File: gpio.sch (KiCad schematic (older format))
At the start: 1 part, among them U1 LFE5U-85F-6BG381C

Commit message: More fixes
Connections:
- net AUDIO_L0 renamed LTDC_TO_FPGA_DE
- net AUDIO_L1 renamed LTDC_TO_FPGA_B6
- net AUDIO_L2 renamed LTDC_TO_FPGA_G4
- net AUDIO_R0 renamed LTDC_TO_FPGA_G2
- net AUDIO_R2 renamed LTDC_TO_FPGA_B5
- net AUDIO_V2 renamed LTDC_TO_FPGA_B4
- net GN10 renamed LTDC_TO_FPGA_B7
- net GN11 renamed LTDC_TO_FPGA_B3
- net GN9 renamed LTDC_TO_FPGA_R6
- net GP11 renamed LTDC_TO_FPGA_G5
- net GP12 renamed LTDC_TO_FPGA_CLK
- net GP9 renamed LTDC_TO_FPGA_G7
- net LED1 renamed LTDC_TO_FPGA_R7
- net LED2 renamed LTDC_TO_FPGA_HSYNC
- net LED3 renamed LTDC_TO_FPGA_VSYNC
- net LED4 renamed LTDC_TO_FPGA_R4
- net LED6 renamed LTDC_TO_FPGA_R5
- net LED7 renamed LTDC_TO_FPGA_R3
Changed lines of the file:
@@
 Text GLabel 4200 4900 0    60   Input ~ 0
 GP13
-Text GLabel 4200 5100 0    60   Input ~ 0
-GP12
 Text GLabel 5700 5100 2    60   Input ~ 0
 GN12
-Text GLabel 5700 4300 2    60   Input ~ 0
-GN11
-Text GLabel 4200 4300 0    60   Input ~ 0
-GP11
-Text GLabel 5700 4500 2    60   Input ~ 0
-GN9
-Text GLabel 4200 4500 0    60   Input ~ 0
-GP9
-Text GLabel 5700 3900 2    60   Input ~ 0
-GN10
 Text GLabel 5700 3700 2    60   Input ~ 0
 GN8
@@
 Text GLabel 4200 2100 0    60   Input ~ 0
 GP3
-Text GLabel 4200 4100 0    60   Input ~ 0
-AUDIO_L0
-Text GLabel 5700 4000 2    60   Input ~ 0
-AUDIO_L1
-Text GLabel 4200 4000 0    60   Input ~ 0
-AUDIO_L2
 Text GLabel 5700 3800 2    60   Input ~ 0
 AUDIO_L3
-Text GLabel 4200 3800 0    60   Input ~ 0
-AUDIO_R0
 Text GLabel 4200 3600 0    60   Input ~ 0
 AUDIO_R1
-Text GLabel 5700 4100 2    60   Input ~ 0
-AUDIO_R2
 Text GLabel 5700 3600 2    60   Input ~ 0
 AUDIO_R3
 Text GLabel 5700 5000 2    60   Input ~ 0
 LED5
-Text GLabel 4200 4700 0    60   Input ~ 0
-LED2
-Text GLabel 4200 4600 0    60   Input ~ 0
-LED3
-Text GLabel 5700 4700 2    60   Input ~ 0
-LED4
-Text GLabel 5700 4400 2    60   Input ~ 0
-LED1
-Text GLabel 5700 4600 2    60   Input ~ 0
-LED6
-Text GLabel 5700 4800 2    60   Input ~ 0
-LED7
 Text Notes 950  7550 0    60   ~ 0
 GPIO route only A/B pairs as those are differential bidirectional\ndon't route C/D pairs to GPIO as those can be differential input only\nBANK0,1 are single-ended (non-differential)
@@
 Text GLabel 4200 2700 0    60   Input ~ 0
 SW4
-Text GLabel 4200 4200 0    60   Input ~ 0
-AUDIO_V3
-Text GLabel 5700 4200 2    60   Input ~ 0
-AUDIO_V2
 Text GLabel 4200 5000 0    60   Input ~ 0
 AUDIO_V1
@@
 NoConn ~ 4200 3100
 NoConn ~ 5700 3000
-Text GLabel 6950 4800 2    60   Input ~ 0
+Text GLabel 5700 4800 2    60   Input ~ 0
 LTDC_TO_FPGA_R3
-Text GLabel 6950 4700 2    60   Input ~ 0
+Text GLabel 5700 4700 2    60   Input ~ 0
 LTDC_TO_FPGA_R4
-Text GLabel 6950 4600 2    60   Input ~ 0
+Text GLabel 5700 4600 2    60   Input ~ 0
 LTDC_TO_FPGA_R5
-Text GLabel 6950 4500 2    60   Input ~ 0
+Text GLabel 5700 4500 2    60   Input ~ 0
 LTDC_TO_FPGA_R6
-Text GLabel 6950 4400 2    60   Input ~ 0
+Text GLabel 5700 4400 2    60   Input ~ 0
 LTDC_TO_FPGA_R7
 Text GLabel 4200 3900 0    60   Input ~ 0
 LTDC_TO_FPGA_G3
-Text GLabel 2550 4000 0    60   Input ~ 0
+Text GLabel 4200 4000 0    60   Input ~ 0
 LTDC_TO_FPGA_G4
-Text GLabel 2550 4300 0    60   Input ~ 0
+Text GLabel 4200 4300 0    60   Input ~ 0
 LTDC_TO_FPGA_G5
 Text GLabel 4200 4400 0    60   Input ~ 0
 LTDC_TO_FPGA_G6
-Text GLabel 2550 4500 0    60   Input ~ 0
+Text GLabel 4200 4500 0    60   Input ~ 0
 LTDC_TO_FPGA_G7
-Text GLabel 6950 3900 2    60   Input ~ 0
+Text GLabel 5700 3900 2    60   Input ~ 0
 LTDC_TO_FPGA_B7
-Text GLabel 6950 4000 2    60   Input ~ 0
+Text GLabel 5700 4000 2    60   Input ~ 0
 LTDC_TO_FPGA_B6
-Text GLabel 6950 4100 2    60   Input ~ 0
+Text GLabel 5700 4100 2    60   Input ~ 0
 LTDC_TO_FPGA_B5
-Text GLabel 6950 4200 2    60   Input ~ 0
+Text GLabel 5700 4200 2    60   Input ~ 0
 LTDC_TO_FPGA_B4
-Text GLabel 6950 4300 2    60   Input ~ 0
+Text GLabel 5700 4300 2    60   Input ~ 0
 LTDC_TO_FPGA_B3
-Text GLabel 2550 3800 0    60   Input ~ 0
+Text GLabel 4200 3800 0    60   Input ~ 0
 LTDC_TO_FPGA_G2
-Text GLabel 2550 5100 0    60   Input ~ 0
+Text GLabel 4200 5100 0    60   Input ~ 0
 LTDC_TO_FPGA_CLK
-Text GLabel 2550 4100 0    60   Input ~ 0
+Text GLabel 4200 4100 0    60   Input ~ 0
 LTDC_TO_FPGA_DE
-Text GLabel 2550 4700 0    60   Input ~ 0
+Text GLabel 4200 4700 0    60   Input ~ 0
 LTDC_TO_FPGA_HSYNC
-Text GLabel 2550 4600 0    60   Input ~ 0
+Text GLabel 4200 4600 0    60   Input ~ 0
 LTDC_TO_FPGA_VSYNC
-Text GLabel 2750 5100 2    60   Input ~ 0
-GP12
-Wire Wire Line
-	2750 5100 2550 5100
-Text GLabel 2650 3800 2    60   Input ~ 0
-AUDIO_R0
-Text GLabel 2650 4000 2    60   Input ~ 0
-AUDIO_L2
-Text GLabel 2650 4100 2    60   Input ~ 0
-AUDIO_L0
-Text GLabel 2650 4300 2    60   Input ~ 0
-GP11
-Text GLabel 2650 4500 2    60   Input ~ 0
-GP9
-Text GLabel 2650 4600 2    60   Input ~ 0
-LED3
-Text GLabel 2650 4700 2    60   Input ~ 0
-LED2
-Wire Wire Line
-	2550 3800 2650 3800
-Wire Wire Line
-	2550 4000 2650 4000
-Wire Wire Line
-	2650 4100 2550 4100
-Wire Wire Line
-	2550 4300 2650 4300
-Wire Wire Line
-	2550 4500 2650 4500
-Wire Wire Line
-	2650 4600 2550 4600
-Wire Wire Line
-	2550 4700 2650 4700
-Text GLabel 6850 3900 0    60   Input ~ 0
-GN10
-Text GLabel 6850 4000 0    60   Input ~ 0
-AUDIO_L1
-Text GLabel 6850 4100 0    60   Input ~ 0
-AUDIO_R2
-Text GLabel 6850 4200 0    60   Input ~ 0
-AUDIO_V2
-Text GLabel 6850 4300 0    60   Input ~ 0
-GN11
-Text GLabel 6850 4400 0    60   Input ~ 0
-LED1
-Text GLabel 6850 4500 0    60   Input ~ 0
-GN9
-Text GLabel 6850 4600 0    60   Input ~ 0
-LED6
-Text GLabel 6850 4700 0    60   Input ~ 0
-LED4
-Text GLabel 6850 4800 0    60   Input ~ 0
-LED7
-Wire Wire Line
-	6850 3900 6950 3900
-Wire Wire Line
-	6850 4000 6950 4000
-Wire Wire Line
-	6850 4100 6950 4100
-Wire Wire Line
-	6850 4200 6950 4200
-Wire Wire Line
-	6850 4300 6950 4300
-Wire Wire Line
-	6850 4400 6950 4400
-Wire Wire Line
-	6850 4500 6950 4500
-Wire Wire Line
-	6850 4600 6950 4600
-Wire Wire Line
-	6850 4700 6950 4700
-Wire Wire Line
-	6850 4800 6950 4800
 Text GLabel 4100 2800 0    60   Input ~ 0
 LTDC_FROM_FPGA_R3
@@
 Text GLabel 5700 2200 2    60   Input ~ 0
 LTDC_FROM_FPGA_R5
+Text GLabel 4200 4200 0    60   Input ~ 0
+AUDIO_V3
 $EndSCHEMATC

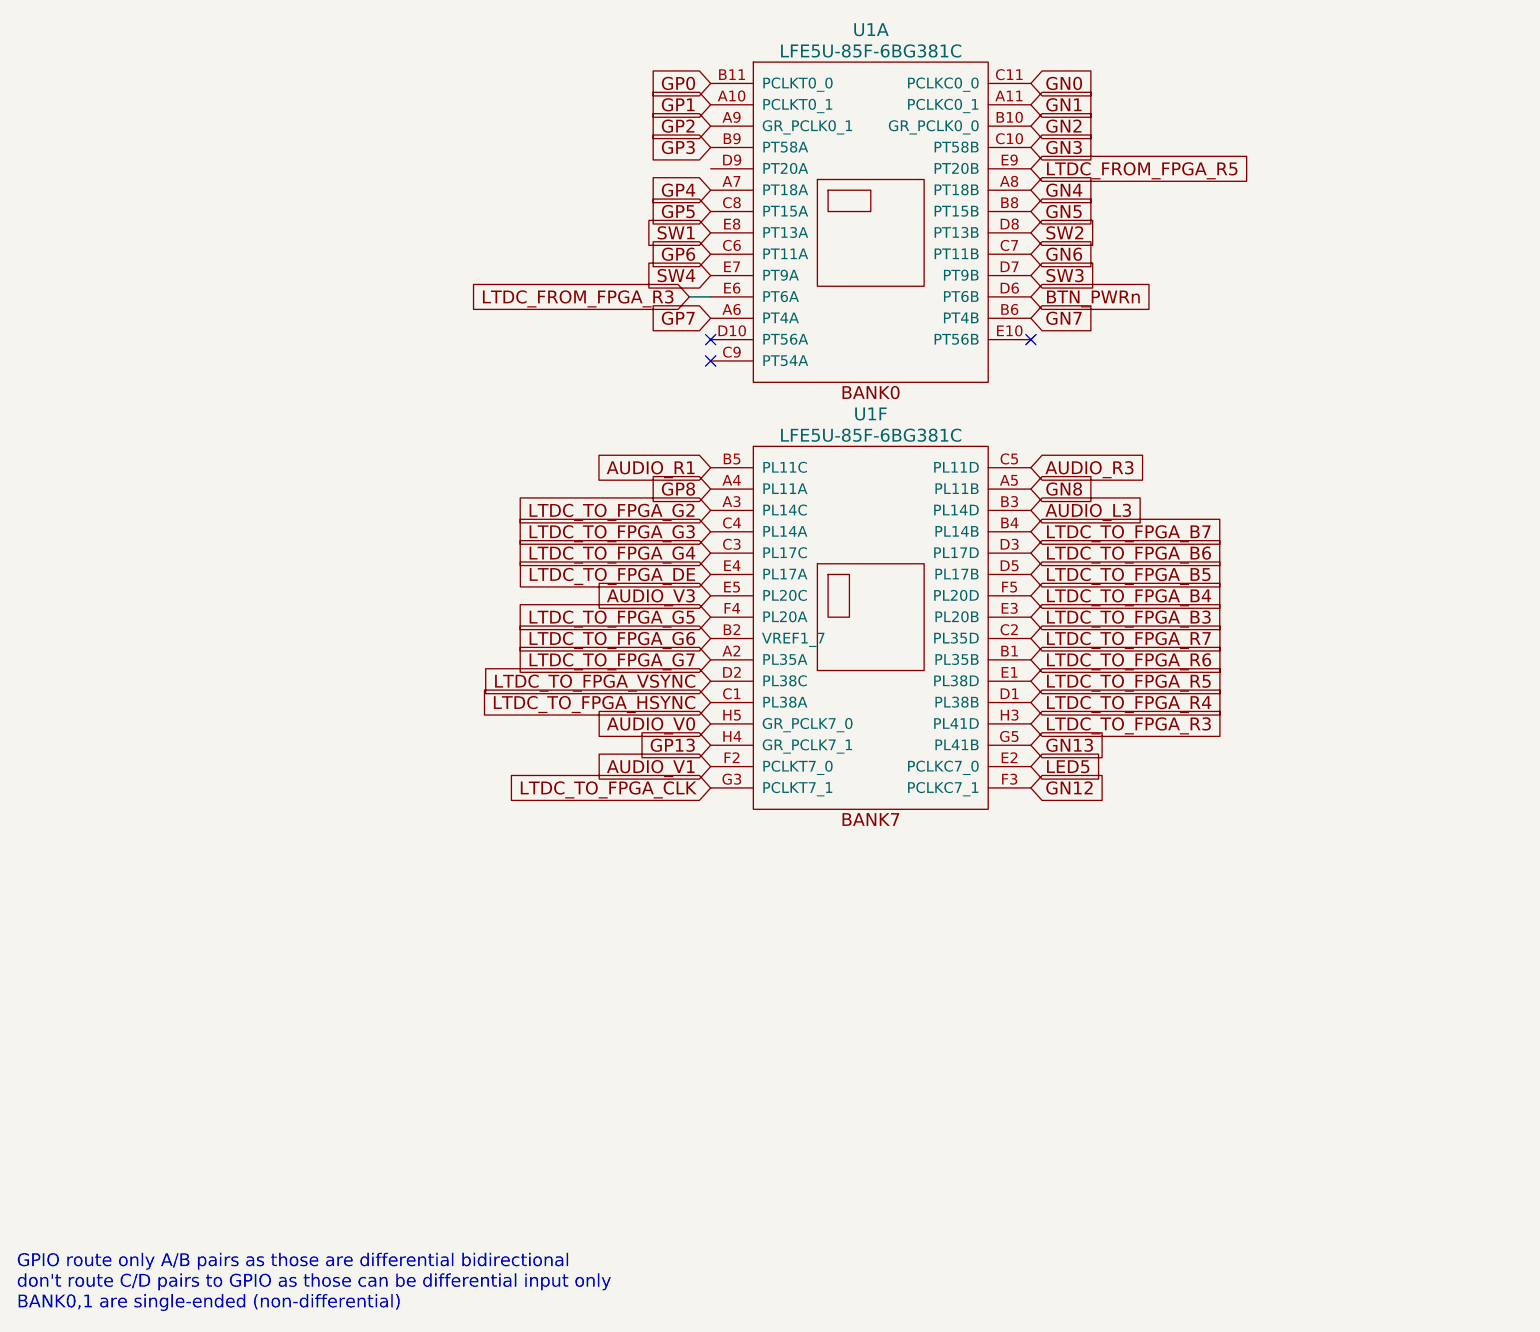
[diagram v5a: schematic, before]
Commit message: Adding all SPI to FPGA resorting LCD TO FPGA
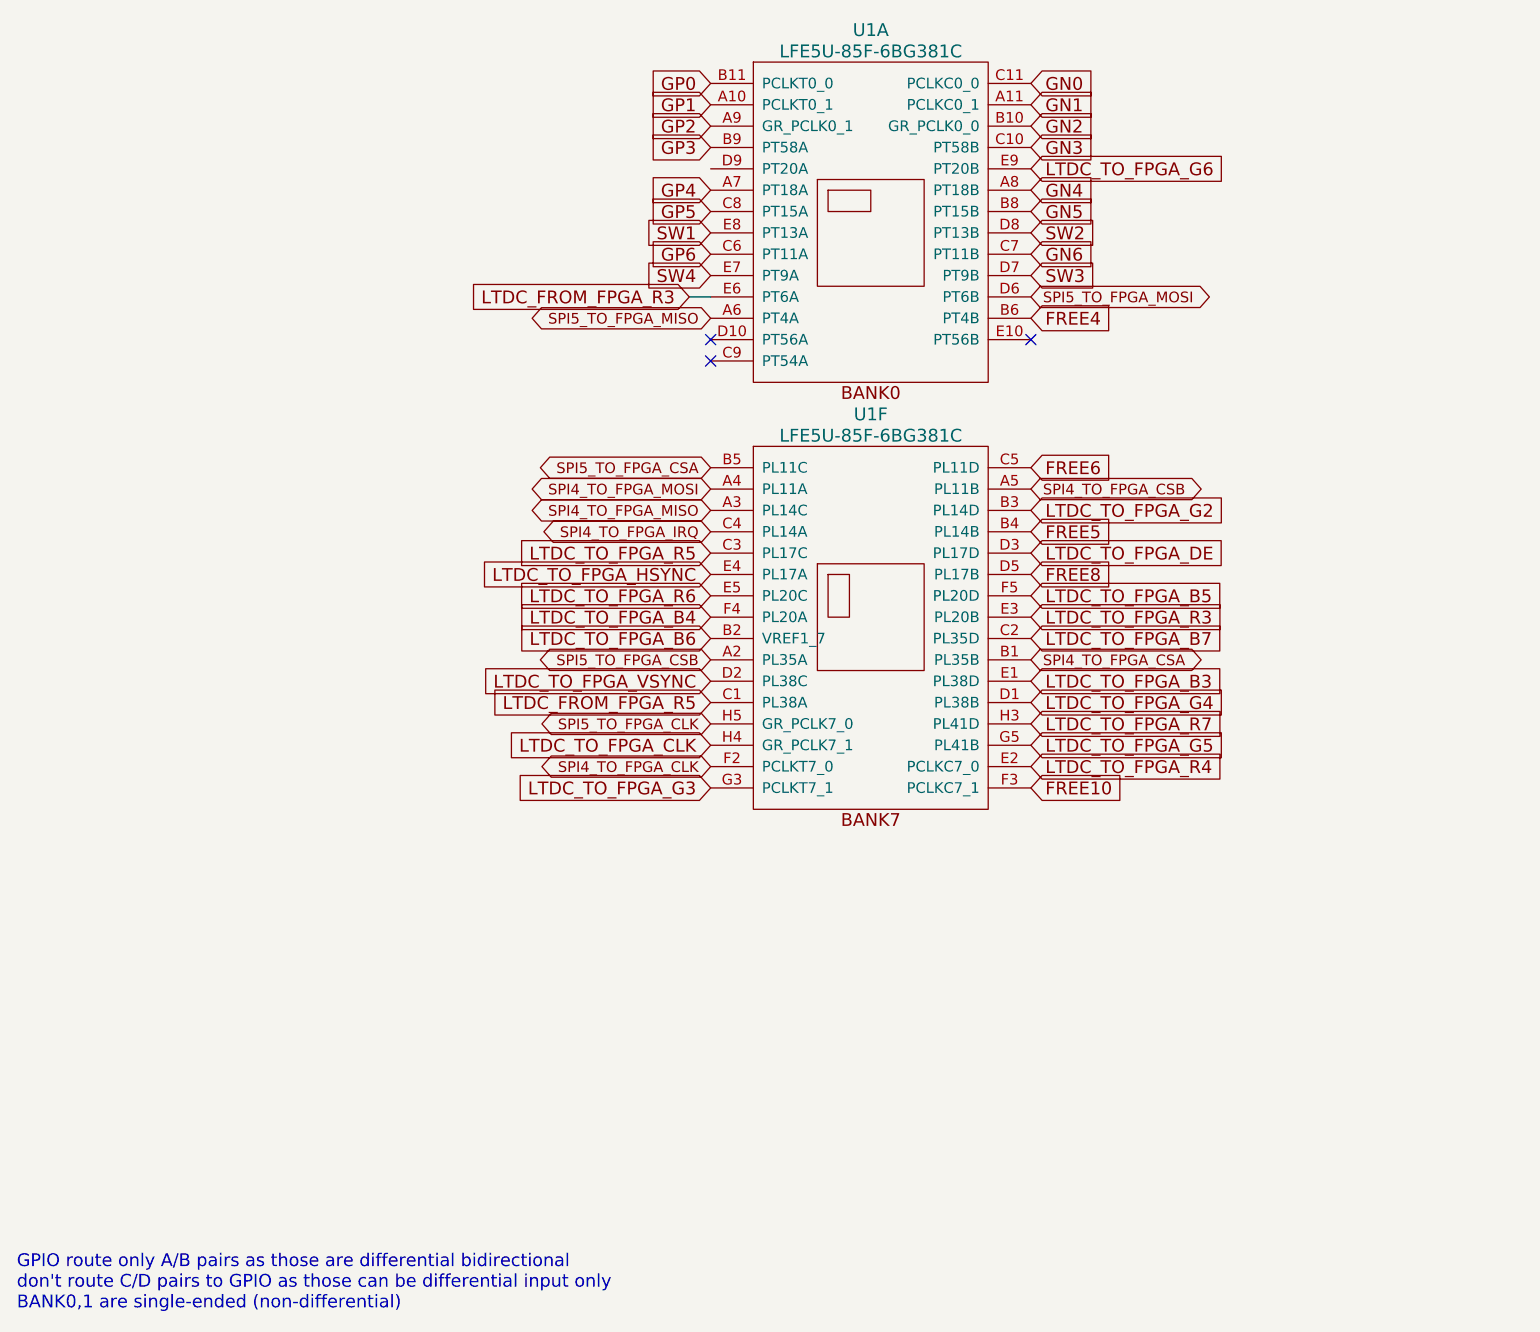
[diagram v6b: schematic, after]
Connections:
- net AUDIO_L3 is gone; now on net LTDC_TO_FPGA_G2: U1.B3 (PL14D)
- net AUDIO_V3 is gone; now on net LTDC_TO_FPGA_R6: U1.E5 (PL20C)
- net GN13 is gone; now on net LTDC_TO_FPGA_G5: U1.G5 (PL41B)
- net GP13 is gone; now on net LTDC_TO_FPGA_CLK: U1.H4 (GR_PCLK7_1)
- net LED5 is gone; now on net LTDC_TO_FPGA_R4: U1.E2 (PCLKC7_0)
- net LTDC_FROM_FPGA_R5: now also U1.C1 (PL38A); no longer U1.E9 (PT20B)
- net LTDC_TO_FPGA_B3: now also U1.E1 (PL38D); no longer U1.E3 (PL20B)
- net LTDC_TO_FPGA_B4: now also U1.F4 (PL20A); no longer U1.F5 (PL20D)
- net LTDC_TO_FPGA_B5: now also U1.F5 (PL20D); no longer U1.D5 (PL17B)
- net LTDC_TO_FPGA_B6: now also U1.B2 (VREF1_7); no longer U1.D3 (PL17D)
- net LTDC_TO_FPGA_B7: now also U1.C2 (PL35D); no longer U1.B4 (PL14B)
- net LTDC_TO_FPGA_CLK: no longer U1.G3 (PCLKT7_1)
- net LTDC_TO_FPGA_DE: now also U1.D3 (PL17D); no longer U1.E4 (PL17A)
- net LTDC_TO_FPGA_G2: no longer U1.A3 (PL14C)
- net LTDC_TO_FPGA_G3: now also U1.G3 (PCLKT7_1); no longer U1.C4 (PL14A)
- net LTDC_TO_FPGA_G4: now also U1.D1 (PL38B); no longer U1.C3 (PL17C)
- net LTDC_TO_FPGA_G5: no longer U1.F4 (PL20A)
- net LTDC_TO_FPGA_G6: now also U1.E9 (PT20B); no longer U1.B2 (VREF1_7)
- net LTDC_TO_FPGA_HSYNC: now also U1.E4 (PL17A); no longer U1.C1 (PL38A)
- net LTDC_TO_FPGA_R3: now also U1.E3 (PL20B); no longer U1.H3 (PL41D)
- net LTDC_TO_FPGA_R4: no longer U1.D1 (PL38B)
- net LTDC_TO_FPGA_R5: now also U1.C3 (PL17C); no longer U1.E1 (PL38D)
- net LTDC_TO_FPGA_R6: no longer U1.B1 (PL35B)
- net LTDC_TO_FPGA_R7: now also U1.H3 (PL41D); no longer U1.C2 (PL35D)
- net AUDIO_R1 renamed SPI5_TO_FPGA_CSA
- net AUDIO_R3 renamed FREE6
- net AUDIO_V0 renamed SPI5_TO_FPGA_CLK
- net AUDIO_V1 renamed SPI4_TO_FPGA_CLK
- net BTN_PWRn renamed SPI5_TO_FPGA_MOSI
- net GN12 renamed FREE10
- net GN7 renamed FREE4
- net GN8 renamed SPI4_TO_FPGA_CSB
- net GP7 renamed SPI5_TO_FPGA_MISO
- net GP8 renamed SPI4_TO_FPGA_MOSI
- net LTDC_TO_FPGA_G7 renamed SPI5_TO_FPGA_CSB
- new net FREE5: U1.B4 (PL14B)
- new net FREE8: U1.D5 (PL17B)
- new net SPI4_TO_FPGA_CSA: U1.B1 (PL35B)
- new net SPI4_TO_FPGA_IRQ: U1.C4 (PL14A)
- new net SPI4_TO_FPGA_MISO: U1.A3 (PL14C)
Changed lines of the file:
@@
 Comment4 ""
 $EndDescr
-Text GLabel 5700 4900 2    60   Input ~ 0
-GN13
-Text GLabel 4200 4900 0    60   Input ~ 0
-GP13
-Text GLabel 5700 5100 2    60   Input ~ 0
-GN12
-Text GLabel 5700 3700 2    60   Input ~ 0
-GN8
-Text GLabel 4200 3700 0    60   Input ~ 0
-GP8
-Text GLabel 5700 2900 2    60   Input ~ 0
-GN7
-Text GLabel 4200 2900 0    60   Input ~ 0
-GP7
 Text GLabel 5700 2600 2    60   Input ~ 0
 GN6
@@
 Text GLabel 4200 2100 0    60   Input ~ 0
 GP3
-Text GLabel 5700 3800 2    60   Input ~ 0
-AUDIO_L3
-Text GLabel 4200 3600 0    60   Input ~ 0
-AUDIO_R1
-Text GLabel 5700 3600 2    60   Input ~ 0
-AUDIO_R3
-Text GLabel 5700 5000 2    60   Input ~ 0
-LED5
 Text Notes 950  7550 0    60   ~ 0
 GPIO route only A/B pairs as those are differential bidirectional\ndon't route C/D pairs to GPIO as those can be differential input only\nBANK0,1 are single-ended (non-differential)
-Text GLabel 5700 2800 2    60   Input ~ 0
-BTN_PWRn
 Text GLabel 4200 2500 0    60   Input ~ 0
 SW1
@@
 Text GLabel 4200 2700 0    60   Input ~ 0
 SW4
-Text GLabel 4200 5000 0    60   Input ~ 0
-AUDIO_V1
-Text GLabel 4200 4800 0    60   Input ~ 0
-AUDIO_V0
 $Comp
 L lfe5bg381:LFE5UM-85F-6BG381C U1
@@
 NoConn ~ 4200 3100
 NoConn ~ 5700 3000
+Text GLabel 5700 4300 2    60   Input ~ 0
+LTDC_TO_FPGA_R3
+Text GLabel 5700 5000 2    60   Input ~ 0
+LTDC_TO_FPGA_R4
+Text GLabel 4200 4000 0    60   Input ~ 0
+LTDC_TO_FPGA_R5
+Text GLabel 4200 4200 0    60   Input ~ 0
+LTDC_TO_FPGA_R6
 Text GLabel 5700 4800 2    60   Input ~ 0
-LTDC_TO_FPGA_R3
+LTDC_TO_FPGA_R7
+Text GLabel 4200 5100 0    60   Input ~ 0
+LTDC_TO_FPGA_G3
 Text GLabel 5700 4700 2    60   Input ~ 0
-LTDC_TO_FPGA_R4
+LTDC_TO_FPGA_G4
+Text GLabel 5700 4900 2    60   Input ~ 0
+LTDC_TO_FPGA_G5
+Text GLabel 5700 2200 2    60   Input ~ 0
+LTDC_TO_FPGA_G6
+Text GLabel 5700 4400 2    60   Input ~ 0
+LTDC_TO_FPGA_B7
+Text GLabel 4200 4400 0    60   Input ~ 0
+LTDC_TO_FPGA_B6
+Text GLabel 5700 4200 2    60   Input ~ 0
+LTDC_TO_FPGA_B5
+Text GLabel 4200 4300 0    60   Input ~ 0
+LTDC_TO_FPGA_B4
 Text GLabel 5700 4600 2    60   Input ~ 0
-LTDC_TO_FPGA_R5
-Text GLabel 5700 4500 2    60   Input ~ 0
-LTDC_TO_FPGA_R6
-Text GLabel 5700 4400 2    60   Input ~ 0
-LTDC_TO_FPGA_R7
-Text GLabel 4200 3900 0    60   Input ~ 0
-LTDC_TO_FPGA_G3
-Text GLabel 4200 4000 0    60   Input ~ 0
-LTDC_TO_FPGA_G4
-Text GLabel 4200 4300 0    60   Input ~ 0
-LTDC_TO_FPGA_G5
-Text GLabel 4200 4400 0    60   Input ~ 0
-LTDC_TO_FPGA_G6
-Text GLabel 4200 4500 0    60   Input ~ 0
-LTDC_TO_FPGA_G7
-Text GLabel 5700 3900 2    60   Input ~ 0
-LTDC_TO_FPGA_B7
+LTDC_TO_FPGA_B3
+Text GLabel 5700 3800 2    60   Input ~ 0
+LTDC_TO_FPGA_G2
+Text GLabel 4200 4900 0    60   Input ~ 0
+LTDC_TO_FPGA_CLK
 Text GLabel 5700 4000 2    60   Input ~ 0
-LTDC_TO_FPGA_B6
-Text GLabel 5700 4100 2    60   Input ~ 0
-LTDC_TO_FPGA_B5
-Text GLabel 5700 4200 2    60   Input ~ 0
-LTDC_TO_FPGA_B4
-Text GLabel 5700 4300 2    60   Input ~ 0
-LTDC_TO_FPGA_B3
-Text GLabel 4200 3800 0    60   Input ~ 0
-LTDC_TO_FPGA_G2
-Text GLabel 4200 5100 0    60   Input ~ 0
-LTDC_TO_FPGA_CLK
+LTDC_TO_FPGA_DE
 Text GLabel 4200 4100 0    60   Input ~ 0
-LTDC_TO_FPGA_DE
-Text GLabel 4200 4700 0    60   Input ~ 0
 LTDC_TO_FPGA_HSYNC
 Text GLabel 4200 4600 0    60   Input ~ 0
@@
 Wire Wire Line
 	4100 2800 4200 2800
-Text GLabel 5700 2200 2    60   Input ~ 0
+Text GLabel 4200 4700 0    60   Input ~ 0
 LTDC_FROM_FPGA_R5
-Text GLabel 4200 4200 0    60   Input ~ 0
-AUDIO_V3
+Text GLabel 5700 2900 2    60   Input ~ 0
+FREE4
+Text GLabel 5700 3600 2    60   Input ~ 0
+FREE6
+Text GLabel 5700 4100 2    60   Input ~ 0
+FREE8
+Text GLabel 5700 5100 2    60   Input ~ 0
+FREE10
+Text GLabel 4200 5000 0    50   BiDi ~ 0
+SPI4_TO_FPGA_CLK
+Text GLabel 5700 3700 2    50   BiDi ~ 0
+SPI4_TO_FPGA_CSB
+Text GLabel 4200 3700 0    50   BiDi ~ 0
+SPI4_TO_FPGA_MOSI
+Text GLabel 4200 3600 0    50   BiDi ~ 0
+SPI5_TO_FPGA_CSA
+Text GLabel 4200 4800 0    50   BiDi ~ 0
+SPI5_TO_FPGA_CLK
+Text GLabel 4200 2900 0    50   BiDi ~ 0
+SPI5_TO_FPGA_MISO
+Text GLabel 5700 2800 2    50   BiDi ~ 0
+SPI5_TO_FPGA_MOSI
+Text GLabel 4200 4500 0    50   BiDi ~ 0
+SPI5_TO_FPGA_CSB
+Text GLabel 5700 4500 2    50   BiDi ~ 0
+SPI4_TO_FPGA_CSA
+Text GLabel 4200 3800 0    50   BiDi ~ 0
+SPI4_TO_FPGA_MISO
+Text GLabel 4200 3900 0    50   BiDi ~ 0
+SPI4_TO_FPGA_IRQ
+Text GLabel 5700 3900 2    60   Input ~ 0
+FREE5
 $EndSCHEMATC
